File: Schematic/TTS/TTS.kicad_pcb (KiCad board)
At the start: 2 copper layers, 112 x 46 mm, 22 parts, among them J1 Screw_Terminal_01x04, J2 Conn_01x15_Female, J3 Conn_01x15_Female, SW1 SW_DIP_x04, U1 ISL81487EIPZ, U2 MLX90614, U3 MLX90614

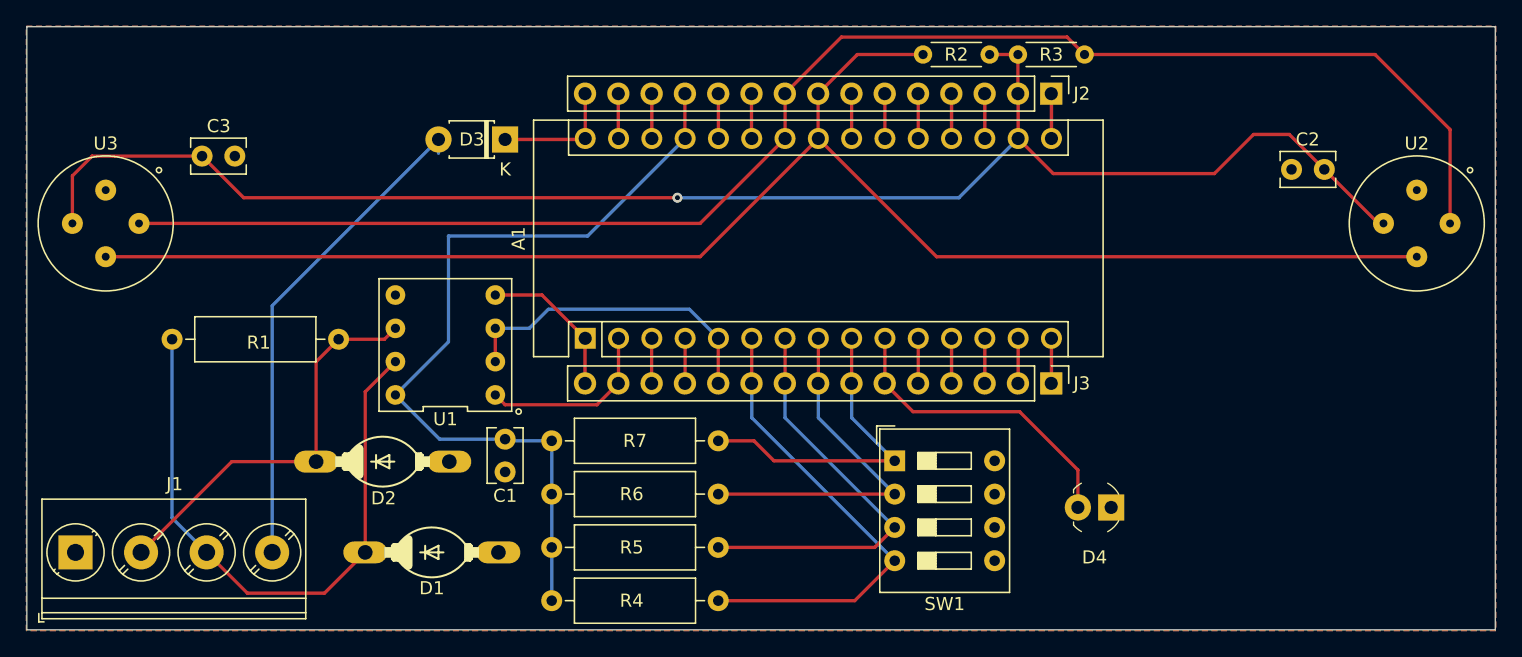
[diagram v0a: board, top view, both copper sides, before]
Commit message: Updating schematic with Oshpark/Digikey order
Updates to add various components and capability.

2.2 Basic Sensor Suite
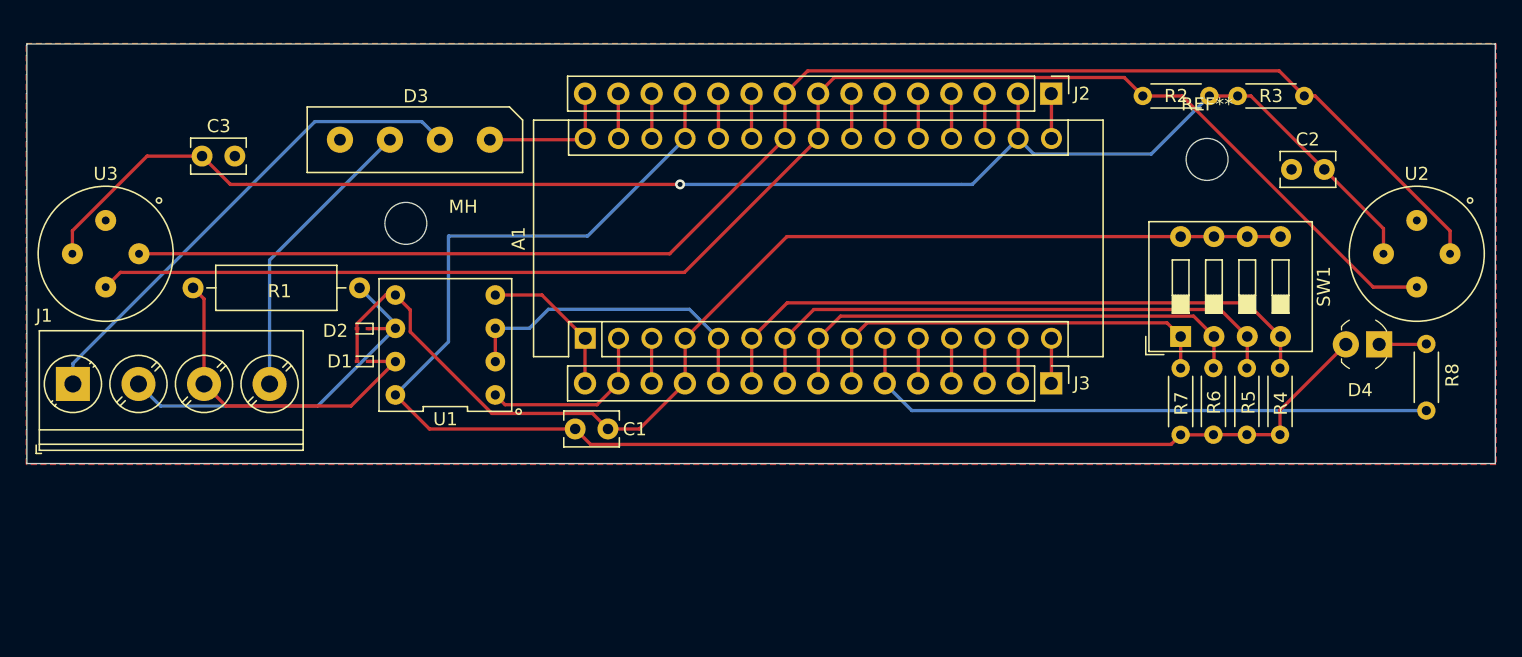
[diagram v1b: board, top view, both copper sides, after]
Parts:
- added MH: MountingHole_3.2mm_M3, MountingHole:MountingHole_3.2mm_M3, F.Cu at (118.4, 87.7)
- added R8: 4.7k, Resistor_THT:R_Axial_DIN0204_L3.6mm_D1.6mm_P5.08mm_Horizontal, F.Cu at (196.2, 102.0)
- added REF**: MountingHole_3.2mm_M3, MountingHole:MountingHole_3.2mm_M3, F.Cu at (179.5, 82.8)
- D1, D2: footprint TTS-UART:DO204-10 -> Diode_SMD:D_SOD-923
- D3: value D -> D_Bridge_+AA-; footprint Diode_THT:D_T-1_P5.08mm_Horizontal -> TTS-UART:KBP306GTB
- R4, R5, R6, R7: value 100 -> 4.7k; footprint Resistor_THT:R_Axial_DIN0309_L9.0mm_D3.2mm_P12.70mm_Horizontal -> Resistor_THT:R_Axial_DIN0204_L3.6mm_D1.6mm_P5.08mm_Horizontal
- moved R4 46.4 mm to (185.1, 98.7), turned to 270 degrees
- moved R5 42.6 mm to (182.6, 98.7), turned to 270 degrees
- moved R6 39.0 mm to (180.0, 98.7), turned to 270 degrees
- moved R7 35.7 mm to (177.5, 98.7), turned to 270 degrees
- moved D4 23.9 mm to (190.1, 96.9)
- moved SW1 23.8 mm to (177.5, 96.3), turned to 90 degrees
- moved R2 17.1 mm to (174.6, 78.0)
- moved R3 17.1 mm to (186.9, 78.0)
- moved D1 15.5 mm to (115.1, 98.2), turned to 180 degrees
- moved J1 12.8 mm to (93.0, 99.9)
- moved D2 10.3 mm to (115.1, 95.7), turned to 180 degrees
- moved D3 6.88 mm to (119.1, 81.3)
- moved C1 5.40 mm to (131.3, 103.4), turned to 0 degrees
- moved R1 4.23 mm to (114.9, 92.6)
- moved U2 2.31 mm to (195.5, 90.0)
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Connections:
- A1 pad 4: /GND_D -> GND1
- C1 pad 2: GND -> GND1
- D1 pad 2: GND -> GND1
- D2 pad 2: GND -> GND1
- D4 pad 1: GND -> Net-(D4-Pad1)
- D4 pad 2: /D7 -> VCC
- J1 pad 1: GND -> Net-(D3-Pad2)
- J1 pad 4: Net-(D3-Pad2) -> Net-(D3-Pad3)
- J3 pad 12: /GND_D -> GND1
- SW1 pad 5: GND -> GND1
- SW1 pad 6: GND -> GND1
- SW1 pad 7: GND -> GND1
- SW1 pad 8: GND -> GND1
- U1 pad 5: GND -> GND1
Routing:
- net GND1: track 0.00 -> 87.5 mm
- net VCC: track 63.9 -> 116.7 mm
- net Net-(D3-Pad3): track 0.00 -> 22.4 mm
- net /D7: track 23.8 -> 45.6 mm
- net Net-(D1-Pad1): track 47.5 -> 26.5 mm
- net /D3: track 36.2 -> 48.4 mm
- net /D4: track 32.0 -> 42.9 mm
- net /D5: track 27.8 -> 37.4 mm
- net /D6: track 24.8 -> 31.9 mm
- net /A4: track 120.1 -> 115.3 mm
- net Net-(D4-Pad1): track 0.00 -> 3.61 mm
- net /GND_D: track 3.44 -> 0.00 mm
- net /A5: track 118.0 -> 114.6 mm
- net VDD: track 121.2 -> 118.3 mm
- net Net-(D2-Pad1): track 30.9 -> 29.1 mm
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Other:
- board size 112 x 46 mm -> 112 x 32 mm
- board text added: "0.2.1"

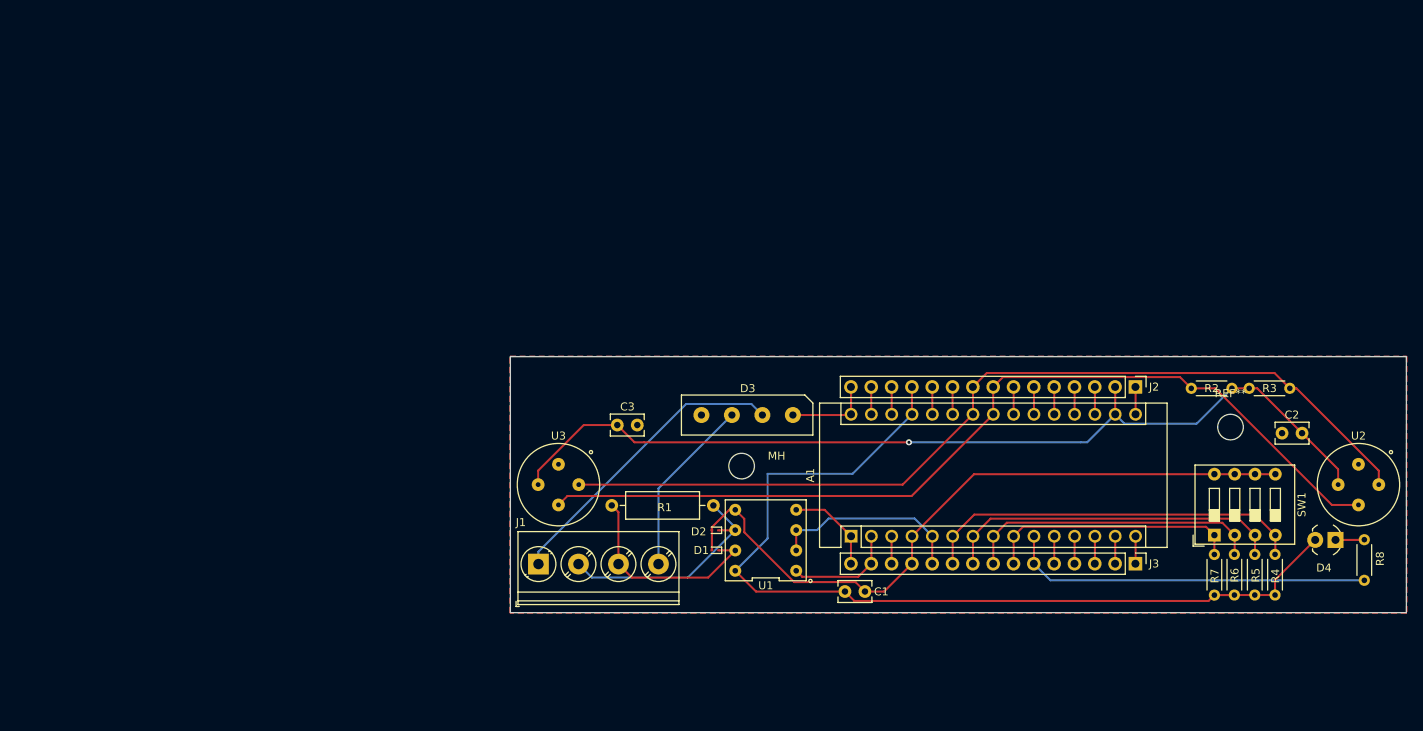
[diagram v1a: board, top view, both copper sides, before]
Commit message: Upadeted PCB design for Logger and for TTS
Mega updated for BLE and reduced in size. Nano shield updated for
MLX90621 array based sensor
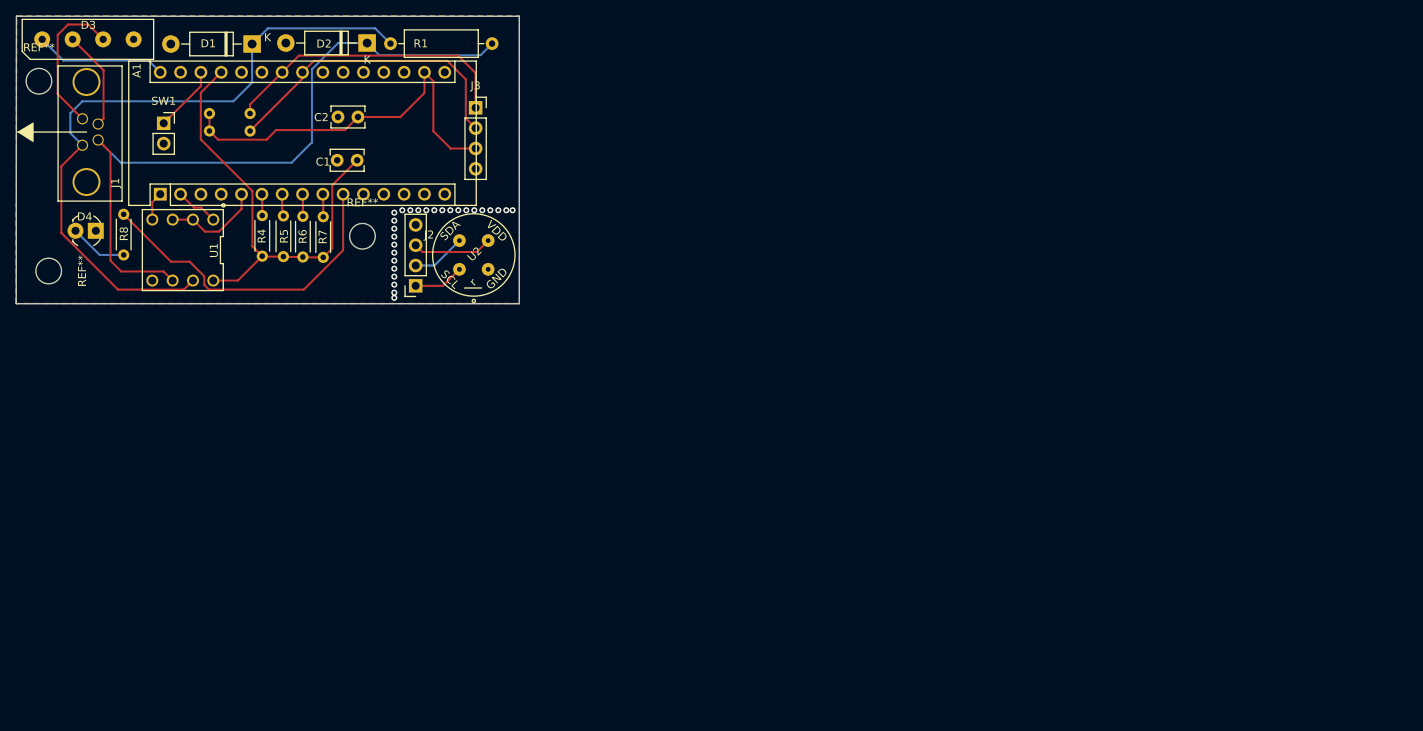
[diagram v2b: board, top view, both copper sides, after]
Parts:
- removed C3: 0.1uF, Capacitor_THT:C_Rect_L4.0mm_W2.5mm_P2.50mm
- removed MH: MountingHole_3.2mm_M3, MountingHole:MountingHole_3.2mm_M3
- removed the REF** at (179.5, 82.8)
- removed U3: MLX90614, TTS-UART:MLX90614ESF-BCC-000-TU
- added REF**: MountingHole_3.2mm_M3, MountingHole:MountingHole_3.2mm_M3, F.Cu at (30.6, 39.6)
- added REF**: MountingHole_3.2mm_M3, MountingHole:MountingHole_3.2mm_M3, F.Cu at (31.8, 63.3)
- added REF**: MountingHole_3.2mm_M3, MountingHole:MountingHole_3.2mm_M3, F.Cu at (71.0, 59.0)
- D1, D2: footprint Diode_SMD:D_SOD-923 -> Diode_THT:D_DO-41_SOD81_P10.16mm_Horizontal
- D4: footprint digikey-kicad-library:LED_3mm_Radial -> Digikey:LED_3mm_Radial
- J1: value Screw_Terminal_01x04 -> Mini-DIN-4; footprint TerminalBlock_Phoenix:TerminalBlock_Phoenix_PT-1,5-4-5.0-H_1x04_P5.00mm_Horizontal -> TTS-URAT:RHT-634-1261-1bottom
- J2, J3: value Conn_01x15_Female -> Conn_01x04_Female; footprint Connector_PinHeader_2.54mm:PinHeader_1x15_P2.54mm_Vertical -> Connector_PinSocket_2.54mm:PinSocket_1x04_P2.54mm_Vertical
- R2, R3: moved to B.Cu
- SW1: value SW_DIP_x04 -> SW_Push; footprint Button_Switch_THT:SW_DIP_SPSTx04_Slide_9.78x12.34mm_W7.62mm_P2.54mm -> Connector_PinSocket_2.54mm:PinSocket_1x02_P2.54mm_Vertical
- U2: value MLX90614 -> MLX90621
- moved R8 161.7 mm to (41.2, 56.2), turned to 270 degrees
- moved D4 159.7 mm to (35.2, 58.3)
- moved SW1 141.1 mm to (46.2, 44.8), turned to 0 degrees
- moved R3 134.4 mm to (57.0, 43.6)
- moved R4 133.5 mm to (58.5, 56.4)
- moved R5 128.6 mm to (61.1, 56.4)
- moved C2 124.5 mm to (70.5, 44.0)
- moved R6 123.9 mm to (63.6, 56.5)
- moved R2 122.0 mm to (57.0, 45.8), turned to 180 degrees
- moved R7 119.1 mm to (66.1, 56.5)
- moved U2 114.2 mm to (84.9, 61.3), turned to 225 degrees
- moved J3 100.2 mm to (85.2, 42.9), turned to 0 degrees
- moved A1 96.4 mm to (45.7, 53.7)
- moved D3 94.8 mm to (36.7, 34.3), turned to 0 degrees
- moved J2 90.8 mm to (77.7, 65.2), turned to 180 degrees
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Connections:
- A1 pad 4: GND1 -> GND
- C1 pad 2: GND1 -> GND
- D1 pad 2: GND1 -> GND
- D2 pad 2: GND1 -> GND
- D4 pad 1: Net-(D4-Pad1) -> GND
- D4 pad 2: VCC -> Net-(D4-Pad2)
- J1 pad 1: Net-(D3-Pad2) -> Net-(D3-Pad3)
- J1 pad 2: Net-(D2-Pad1) -> Net-(D3-Pad2)
- J1 pad 4: Net-(D3-Pad3) -> Net-(D2-Pad1)
- J2 pad 1: /D13 -> /A5
- J2 pad 2: VDD -> /A4
- J2 pad 3: /REF -> VDD
- J2 pad 4: /A0 -> GND
- J3 pad 1: /D12 -> /A5
- J3 pad 2: /D11 -> /A4
- J3 pad 3: /D10 -> VDD
- J3 pad 4: /D9 -> GND
- R8 pad 2: Net-(D4-Pad1) -> Net-(D4-Pad2)
- SW1 pad 1: /D6 -> /RST_A
- SW1 pad 2: /D5 -> GND
- U1 pad 5: GND1 -> GND
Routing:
- net GND1: track 87.5 -> 0.00 mm
- net /A5: track 114.6 -> 43.4 mm
- net /A4: track 115.3 -> 45.4 mm
- net VCC: track 116.7 -> 56.2 mm
- net VDD: track 118.3 -> 58.5 mm, vias 1 -> 0
- net Net-(D2-Pad1): track 29.1 -> 88.7 mm
- net Net-(D1-Pad1): track 26.5 -> 84.6 mm
- net /D3: track 48.4 -> 2.69 mm
- net /D4: track 42.9 -> 2.78 mm
- net /D5: track 37.4 -> 2.79 mm
- net /D6: track 31.9 -> 2.84 mm
- net Net-(D3-Pad2): track 37.8 -> 12.5 mm
- net /D2: track 24.5 -> 12.3 mm
- net /RX: track 13.8 -> 5.40 mm
- net /TX: track 11.7 -> 3.59 mm
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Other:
- board size 112 x 32 mm -> 62.9 x 35.9 mm
- board text added: "0.2.1v3"
- board text removed: "0.2.1"

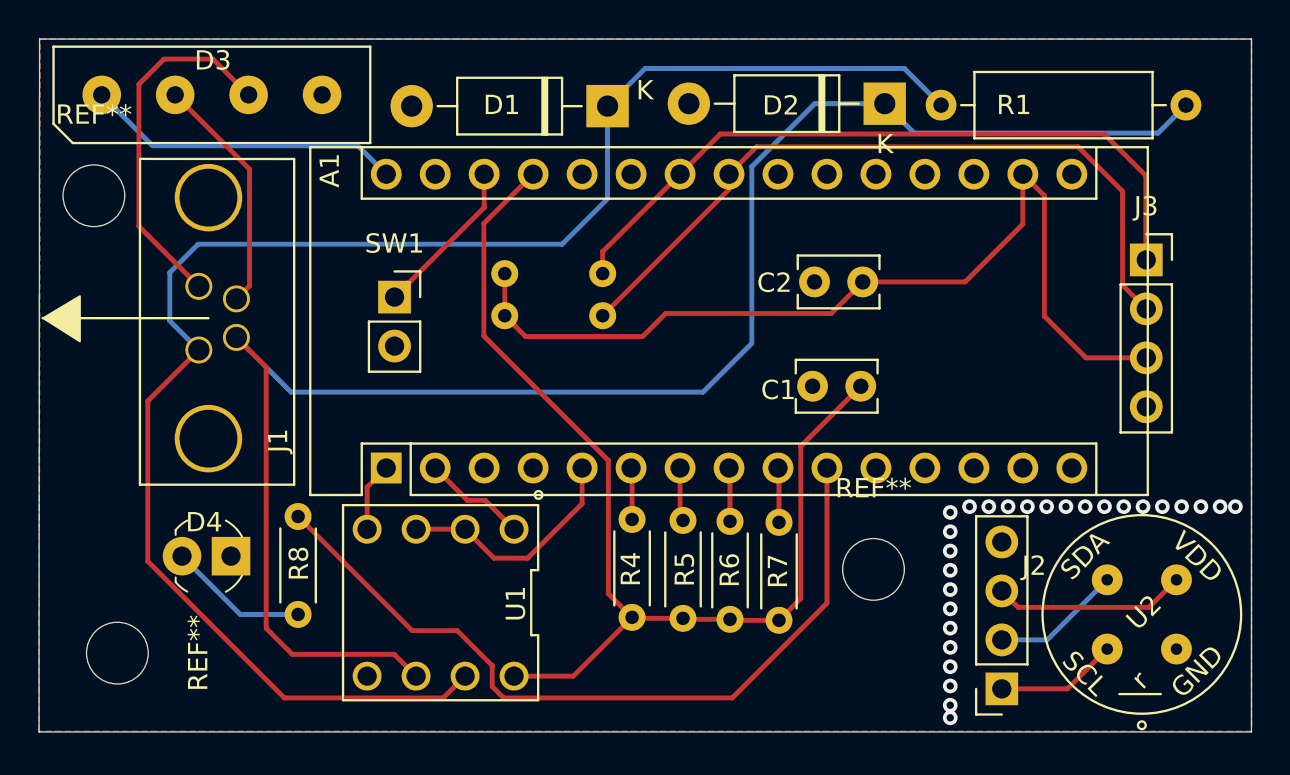
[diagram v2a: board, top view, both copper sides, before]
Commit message: Verion 4 PCB and Code
Updated PCB layout for version 4; for both TTS and Logger.
Updated code to asign ID to TTS and to send data via BT
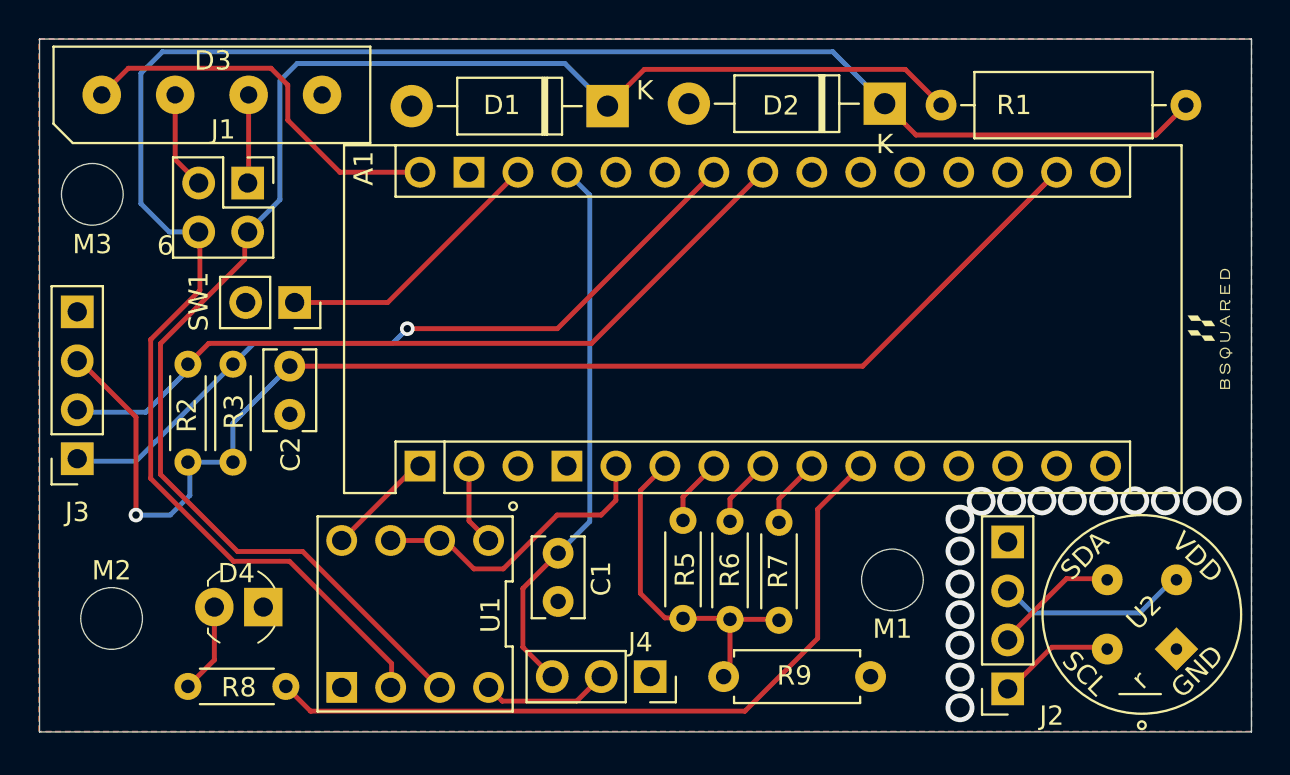
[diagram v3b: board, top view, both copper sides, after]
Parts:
- removed R4: 4.7k, Resistor_THT:R_Axial_DIN0204_L3.6mm_D1.6mm_P5.08mm_Horizontal
- added G***: LOGO, BSquared:BSquaredFP_6mm, B.Cu at (89.4, 61.2)
- added G***: LOGO, BSquared:BSquaredFP_6mm, B.Cu at (88.4, 46.5)
- added G***: LOGO, BSquared:BSquaredFP_6mm, F.Cu at (88.4, 46.5)
- added J4: Jumper, Connector_PinSocket_2.54mm:PinSocket_1x03_P2.54mm_Vertical, F.Cu at (59.4, 64.5)
- added R9: 10K, Resistor_THT:R_Axial_DIN0207_L6.3mm_D2.5mm_P7.62mm_Horizontal, F.Cu at (63.2, 64.5)
- J1: footprint TTS-URAT:RHT-634-1261-1bottom -> Connector_PinSocket_2.54mm:PinSocket_2x02_P2.54mm_Vertical
- R2, R3: moved to F.Cu
- moved J3 56.4 mm to (29.7, 53.2), turned to 180 degrees
- moved C2 30.0 mm to (40.7, 48.4), turned to 270 degrees
- moved R2 21.7 mm to (35.5, 48.3), turned to 270 degrees
- moved R3 19.7 mm to (37.8, 48.3), turned to 270 degrees
- moved C1 17.9 mm to (54.7, 58.1), turned to 270 degrees
- moved R8 8.84 mm to (40.5, 65.0), turned to 180 degrees
- moved J1 7.30 mm to (38.6, 38.9), turned to 0 degrees
- moved SW1 5.19 mm to (41.0, 45.1), turned to 270 degrees
- moved D4 3.13 mm to (36.8, 60.9)
- moved M2 1.82 mm to (31.5, 61.5)
- moved A1 1.76 mm to (47.5, 53.6)
- moved U1 1.44 mm to (47.2, 61.3)
- moved M1 1.12 mm to (72.0, 59.5)
- moved J2 0.30 mm to (78.0, 65.2)
- moved M3 0.11 mm to (30.5, 39.5)
- renumbered REF** to M1, REF** to M2, REF** to M3
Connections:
- R5 pad 2: VCC -> /D3
- R6 pad 2: VCC -> /D3
- R7 pad 2: VCC -> /D3
- U1 pad 8: VCC -> Net-(J4-Pad2)
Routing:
- net VDD: track 58.5 -> 87.1 mm, vias 0 -> 1
- net VCC: track 56.2 -> 28.7 mm
- net /D3: track 2.69 -> 18.1 mm
- net Net-(D3-Pad3): track 18.8 -> 4.59 mm
- net Net-(D2-Pad1): track 88.7 -> 98.7 mm
- net Net-(D3-Pad2): track 12.5 -> 5.74 mm
- net Net-(J4-Pad2): track 0.00 -> 6.66 mm
- net /RST_A: track 8.30 -> 14.4 mm
- net Net-(D1-Pad1): track 84.6 -> 79.0 mm
- net /VIN: track 16.5 -> 20.4 mm
- net /D2: track 12.3 -> 15.3 mm
- net Net-(D4-Pad2): track 7.27 -> 4.68 mm
- net /A4: track 45.4 -> 47.8 mm
- net /A5: track 43.4 -> 45.6 mm, vias 0 -> 1
- net /TX: track 3.59 -> 5.66 mm
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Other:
- board text added: "0.2.1v4"
- board text added: "6"
- board text removed: "0.2.1v3"
